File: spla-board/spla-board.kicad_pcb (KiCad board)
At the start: 4 copper layers, 165 x 107 mm, 285 parts, among them J1 USB_B_Micro, J12 J_POWER, J13 J_ANALOG, J14 J_AREF, J15 J_DPULL, J2 J_JTAG, J3 J_BODGE, J5 J_PPURESET, J6 J_SAMPLE, J7 Barrel_Jack, J8 J_AREF_AMP, J9 J_EXTRA, SW1 PTS645, SW2 SW_DPDT_x2, U1 LFE5U-45F-BG256, U10 SNES_PPU1, U11 SNES_PPU2, U12 VRAM, U13 VRAM, U14 TLV73311PDBV, U15 74LVC8T245, U16 74LVC8T245, U17 74LVC8T245, U2 FT2232H, U20 74LVC8T245, U22 74LVC8T245, U23 74LVC8T245, U24 74LVC8T245, U25 74LVC8T245, U26 74LVC8T245, U27 74LVC8T245, U28 74LVC8T245, U29 74LVC8T245, U3 93LC66B, U30 74LVC8T245, U31 74LVC8T245, U32 74LVC8T245, U4 74LVC1G17, U5 74LVC1G17, U51 ADC1173, U52 ADC1173, U53 ADC1173, U61 LMH6611, U62 LMH6611, U63 LMH6611, U7 ST1S10PHR, U74 LMH6611, U75 LMH6611, U76 TLV73333PDBV, U8 ST1S10PHR, U9 TLV73325PDBV, X1 FT5HNBPK12.0-T1

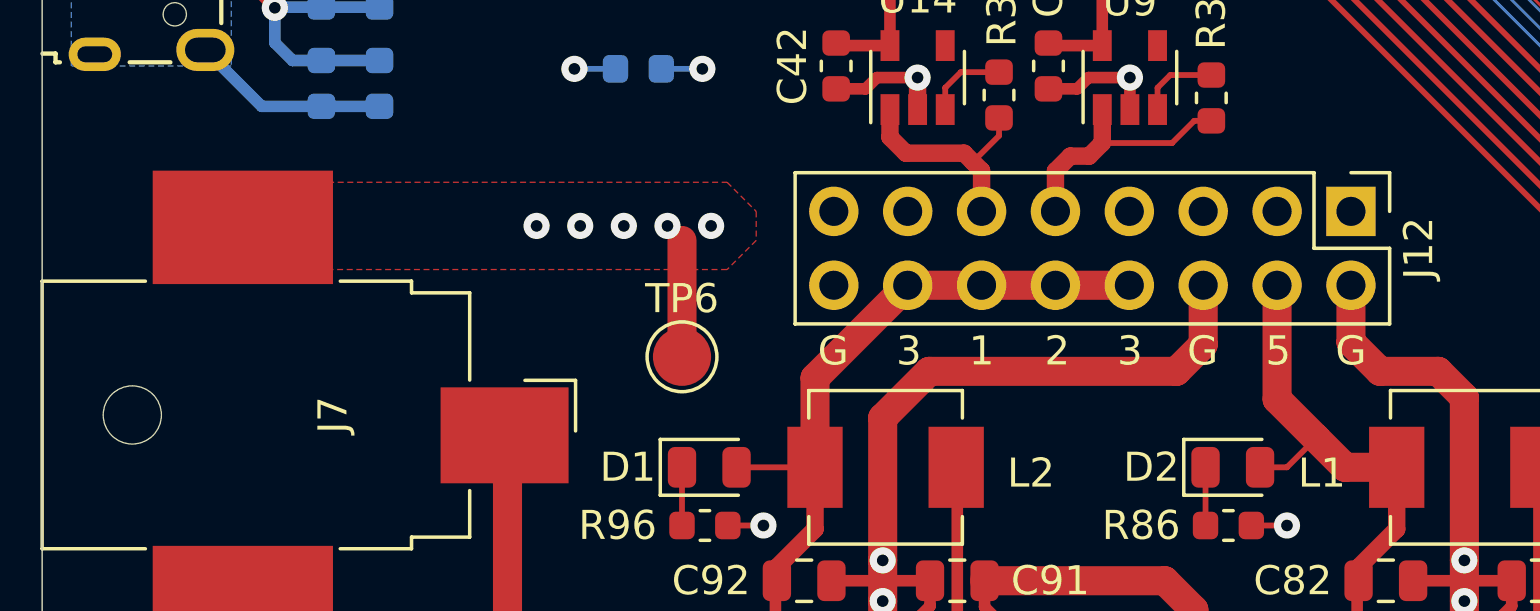
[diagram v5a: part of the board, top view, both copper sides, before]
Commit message: pcb: Remove GND via stitching, connect via J12 instead.
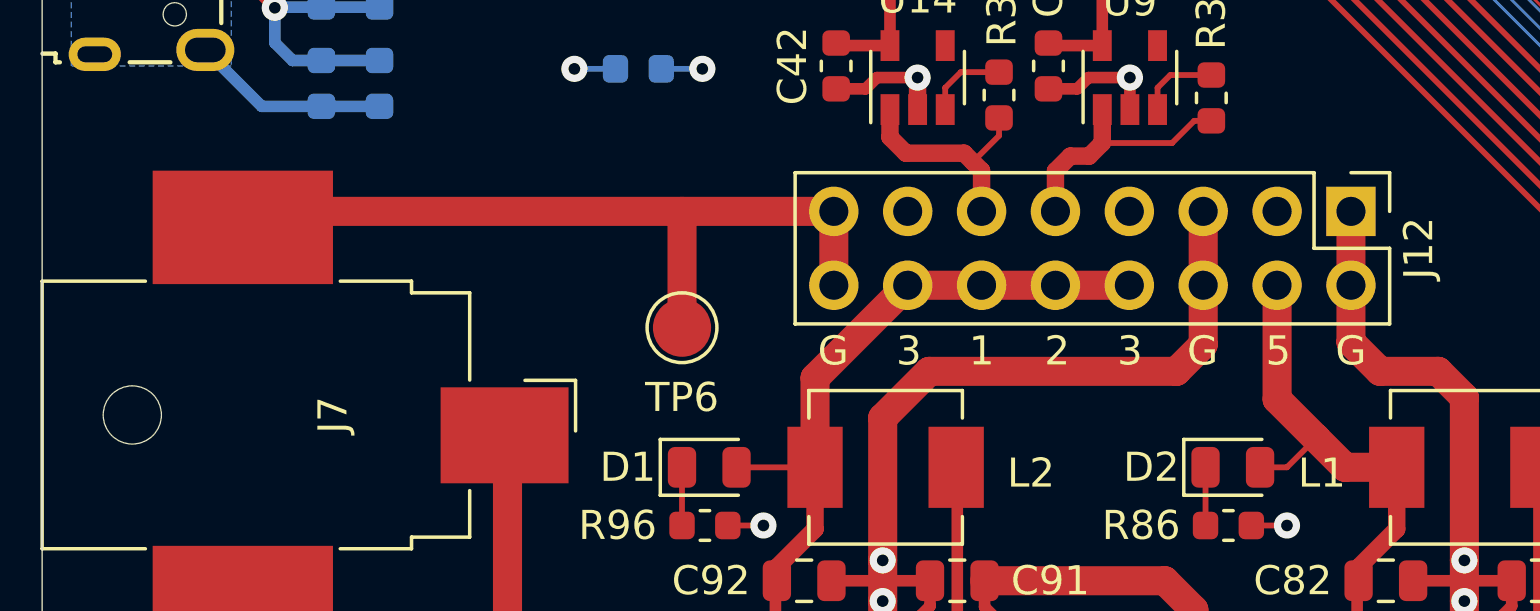
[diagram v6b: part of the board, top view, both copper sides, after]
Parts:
- moved TP6 1.00 mm to (75.0, 130.0)
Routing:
- net GND: track 526.5 -> 554.7 mm, vias 162 -> 157
- removed copper zone on F.Cu, net GND
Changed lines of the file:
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@@
     (thickness 1.6)
     (drawings 70)
-    (tracks 4560)
+    (tracks 4559)
     (zones 0)
     (modules 285)
@@
   )
   (module TestPoint:TestPoint_Pad_D2.0mm (layer F.Cu)
-    (at 75 131)
+    (at 75 130)
     (descr "SMD pad as test Point, diameter 2.0mm")
     (tags "test point SMD pad")
     (attr virtual)
-    (fp_text reference TP6 (at 0 -1.998) (layer F.SilkS)
+    (fp_text reference TP6 (at 0 2.4) (layer F.SilkS)
       (effects (font (size 1 1) (thickness 0.15)))
     )
@@
   (segment (start 90.2 106.8) (end 90.6 106.4) (width 0.4) (layer B.Cu) (net 1))
   (segment (start 90.2 107.4) (end 90.2 106.8) (width 0.4) (layer B.Cu) (net 1))
-  (segment (start 76 126.5) (end 76 126.5) (width 1) (layer F.Cu) (net 1))
   (segment (start 163.6875 85.2) (end 163.8 85.0875) (width 0.2) (layer B.Cu) (net 1))
   (segment (start 135 99.4) (end 133 99.4) (width 0.1) (layer F.Cu) (net 1))
@@
   (segment (start 61 120.2) (end 61 119) (width 0.4) (layer B.Cu) (net 1))
   (segment (start 61.6125 120.8125) (end 61 120.2) (width 0.4) (layer B.Cu) (net 1))
-  (via (at 76 126.5) (size 0.9) (drill 0.4) (layers F.Cu B.Cu) (net 1))
-  (via (at 74.5 126.5) (size 0.9) (drill 0.4) (layers F.Cu B.Cu) (net 1))
-  (via (at 73 126.5) (size 0.9) (drill 0.4) (layers F.Cu B.Cu) (net 1))
-  (via (at 71.5 126.5) (size 0.9) (drill 0.4) (layers F.Cu B.Cu) (net 1))
-  (via (at 70 126.5) (size 0.9) (drill 0.4) (layers F.Cu B.Cu) (net 1))
   (segment (start 77.7 115.0875) (end 77.8125 115.2) (width 0.2) (layer F.Cu) (net 1))
   (segment (start 77.7 113.7) (end 77.7 115.0875) (width 0.2) (layer F.Cu) (net 1))
@@
   (segment (start 135.8875 134.4125) (end 135.8875 134.4125) (width 0.2) (layer B.Cu) (net 1))
   (via (at 135.8875 134.4125) (size 0.9) (drill 0.4) (layers F.Cu B.Cu) (net 1))
-  (segment (start 75 127) (end 75 131) (width 1) (layer F.Cu) (net 1))
   (segment (start 61.9 99.475) (end 61.9 101) (width 0.2) (layer B.Cu) (net 1))
   (segment (start 64.5 103.6) (end 67.4 103.6) (width 0.2) (layer B.Cu) (net 1))
   (segment (start 61.9 101) (end 64.5 103.6) (width 0.2) (layer B.Cu) (net 1))
+  (segment (start 60.45 126) (end 59.9 126.55) (width 1) (layer F.Cu) (net 1))
+  (segment (start 80.22 126) (end 60.45 126) (width 1) (layer F.Cu) (net 1))
+  (segment (start 75 126) (end 75 130) (width 1) (layer F.Cu) (net 1))
+  (segment (start 80.22 126) (end 80.22 128.54) (width 1) (layer F.Cu) (net 1))
+  (segment (start 92.92 126) (end 92.92 128.54) (width 1) (layer F.Cu) (net 1))
+  (segment (start 98 126) (end 98 128.54) (width 1) (layer F.Cu) (net 1))
   (via (at 134.3 134.4) (size 0.9) (drill 0.4) (layers F.Cu B.Cu) (net 2))
   (via (at 96.2 102.4) (size 0.45) (drill 0.2) (layers F.Cu B.Cu) (net 2))
@@
       )
     )
-  )
-  (zone (net 1) (net_name GND) (layer F.Cu) (hatch edge 0.508)
-    (connect_pads (clearance 0.508))
-    (min_thickness 0.254)
-    (fill yes (arc_segments 32) (thermal_gap 0.508) (thermal_bridge_width 0.508))
-    (polygon
-      (pts
-        (xy 77.550858 127) (xy 76.550858 128) (xy 57.550858 128) (xy 57.550858 125) (xy 76.550858 125)
-        (xy 77.550858 126)
-      )
-    )

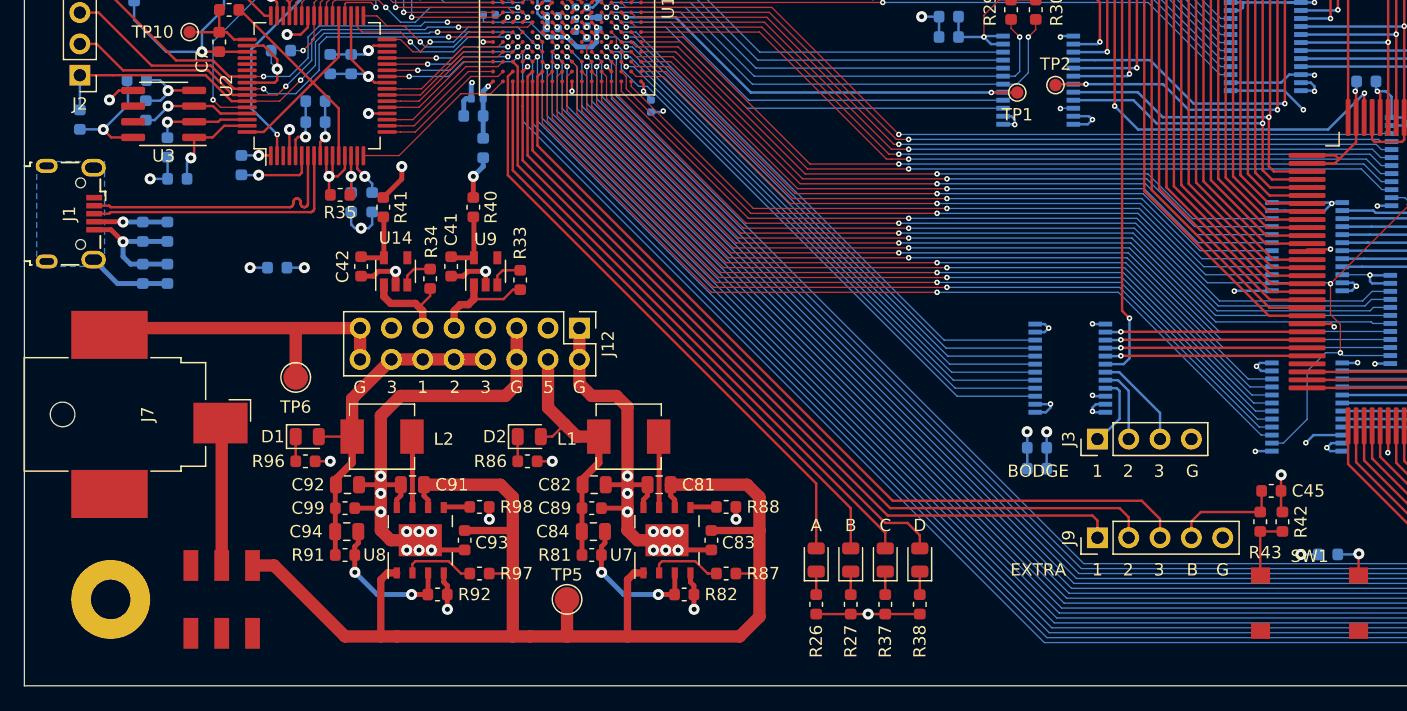
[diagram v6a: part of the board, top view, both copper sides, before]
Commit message: schematic/pcb: Remove bogus JTAG TMS pullup.
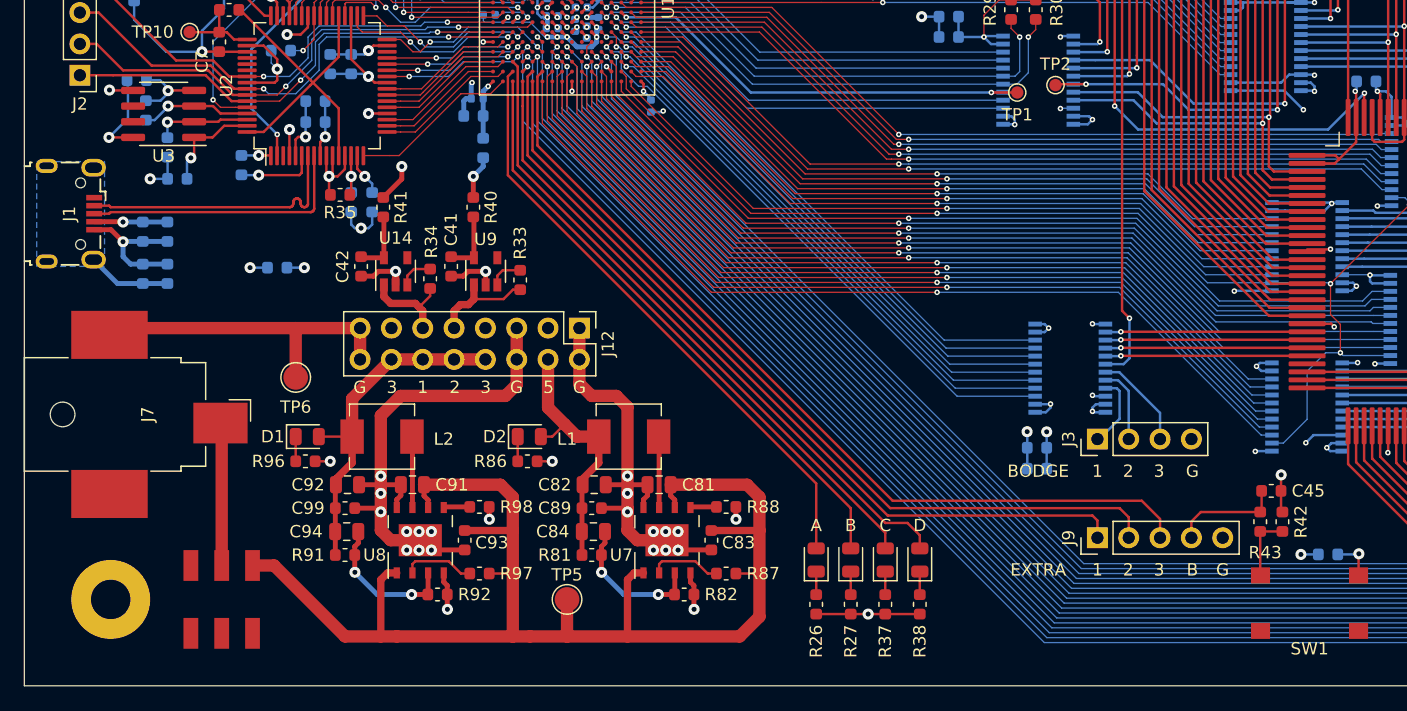
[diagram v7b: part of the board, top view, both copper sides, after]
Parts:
- removed R13: 10k, Resistor_SMD:R_0603_1608Metric
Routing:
- net JTAG_TMS: track 40.6 -> 37.8 mm
- net +3V3: track 158.0 -> 155.8 mm
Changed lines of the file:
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@@
     (thickness 1.6)
     (drawings 70)
-    (tracks 4559)
+    (tracks 4555)
     (zones 0)
-    (modules 285)
+    (modules 284)
     (nets 455)
   )
@@
   )
   (setup
-    (last_trace_width 1)
+    (last_trace_width 0.2)
     (user_trace_width 0.1)
     (user_trace_width 0.2)
@@
   (module SPLA:PTS645-SMTR92 (layer F.Cu)
     (at 157.2 148.3)
-    (fp_text reference SW1 (at 0 -3.8) (layer F.SilkS)
+    (fp_text reference SW1 (at 0 3.7) (layer F.SilkS)
       (effects (font (size 1 1) (thickness 0.15)))
     )
@@
     )
   )
-  (module Resistor_SMD:R_0603_1608Metric (layer B.Cu)
-    (at 57.5 109.1 90)
-    (descr "Resistor SMD 0603 (1608 Metric), square (rectangular) end terminal, IPC_7351 nominal, (Body size source: http://www.tortai-tech.com/upload/download/2011102023233369053.pdf), generated with kicad-footprint-generator")
-    (tags resistor)
-    (attr smd)
-    (fp_text reference R13 (at 0 -1.524 90) (layer B.SilkS)
-      (effects (font (size 1 1) (thickness 0.15)) (justify mirror))
-    )
-    (fp_text value 10k (at 0 -1.43 90) (layer B.Fab)
-      (effects (font (size 1 1) (thickness 0.15)) (justify mirror))
-    )
-    (fp_line (start -0.8 -0.4) (end -0.8 0.4) (layer B.Fab) (width 0.1))
-    (fp_line (start -0.8 0.4) (end 0.8 0.4) (layer B.Fab) (width 0.1))
-    (fp_line (start 0.8 0.4) (end 0.8 -0.4) (layer B.Fab) (width 0.1))
-    (fp_line (start 0.8 -0.4) (end -0.8 -0.4) (layer B.Fab) (width 0.1))
-    (fp_line (start -0.162779 0.51) (end 0.162779 0.51) (layer B.SilkS) (width 0.12))
-    (fp_line (start -0.162779 -0.51) (end 0.162779 -0.51) (layer B.SilkS) (width 0.12))
-    (fp_line (start -1.48 -0.73) (end -1.48 0.73) (layer B.CrtYd) (width 0.05))
-    (fp_line (start -1.48 0.73) (end 1.48 0.73) (layer B.CrtYd) (width 0.05))
-    (fp_line (start 1.48 0.73) (end 1.48 -0.73) (layer B.CrtYd) (width 0.05))
-    (fp_line (start 1.48 -0.73) (end -1.48 -0.73) (layer B.CrtYd) (width 0.05))
-    (fp_text user %R (at 0 0 90) (layer B.Fab)
-      (effects (font (size 0.4 0.4) (thickness 0.06)) (justify mirror))
-    )
-    (pad 2 smd roundrect (at 0.7875 0 90) (size 0.875 0.95) (layers B.Cu B.Paste B.Mask) (roundrect_rratio 0.25)
-      (net 6 JTAG_TMS))
-    (pad 1 smd roundrect (at -0.7875 0 90) (size 0.875 0.95) (layers B.Cu B.Paste B.Mask) (roundrect_rratio 0.25)
-      (net 2 +3V3))
-    (model ${KISYS3DMOD}/Resistor_SMD.3dshapes/R_0603_1608Metric.wrl
-      (at (xyz 0 0 0))
-      (scale (xyz 1 1 1))
-      (rotate (xyz 0 0 0))
-    )
-  )
   (module Resistor_SMD:R_0603_1608Metric (layer F.Cu)
     (at 109.9 145.9 180)
@@
   (segment (start 79.4875 104.1875) (end 79.4875 100.675) (width 0.2) (layer F.Cu) (net 1))
   (segment (start 80.9 105.6) (end 79.4875 104.1875) (width 0.2) (layer F.Cu) (net 1))
-  (via (at 59.9 107.5) (size 0.9) (drill 0.4) (layers F.Cu B.Cu) (net 1))
-  (segment (start 61.8165 106.731) (end 60.669 106.731) (width 0.2) (layer F.Cu) (net 1))
-  (segment (start 60.669 106.731) (end 59.9 107.5) (width 0.2) (layer F.Cu) (net 1))
   (segment (start 98.615 100.815) (end 98.6 100.8) (width 0.4) (layer B.Cu) (net 1))
   (segment (start 99.55 100.815) (end 98.615 100.815) (width 0.4) (layer B.Cu) (net 1))
@@
   (segment (start 92.92 126) (end 92.92 128.54) (width 1) (layer F.Cu) (net 1))
   (segment (start 98 126) (end 98 128.54) (width 1) (layer F.Cu) (net 1))
+  (segment (start 59.931 106.731) (end 61.8165 106.731) (width 0.2) (layer F.Cu) (net 1))
+  (via (at 59.9 106.7) (size 0.9) (drill 0.4) (layers F.Cu B.Cu) (net 1))
+  (segment (start 59.9 106.7) (end 59.931 106.731) (width 0.2) (layer F.Cu) (net 1))
   (via (at 134.3 134.4) (size 0.9) (drill 0.4) (layers F.Cu B.Cu) (net 2))
   (via (at 96.2 102.4) (size 0.45) (drill 0.2) (layers F.Cu B.Cu) (net 2))
@@
   (segment (start 75.7 121.1) (end 74.2875 121.1) (width 0.2) (layer B.Cu) (net 2))
   (via (at 75.7 121.1) (size 0.9) (drill 0.4) (layers F.Cu B.Cu) (net 2))
-  (segment (start 59.3875 109.8875) (end 57.5 109.8875) (width 0.2) (layer B.Cu) (net 2))
-  (segment (start 61.325 105.925) (end 61.325 105.9) (width 0.2) (layer B.Cu) (net 2))
-  (segment (start 59.4 109.9) (end 60.041 110.541) (width 0.2) (layer F.Cu) (net 2))
-  (via (at 59.4 109.9) (size 0.9) (drill 0.4) (layers F.Cu B.Cu) (net 2))
-  (segment (start 59.4 109.9) (end 59.3875 109.8875) (width 0.2) (layer B.Cu) (net 2))
-  (segment (start 60.041 110.541) (end 61.8165 110.541) (width 0.2) (layer F.Cu) (net 2))
-  (segment (start 59.4 109.9) (end 61.4 107.9) (width 0.2) (layer B.Cu) (net 2))
-  (segment (start 61.4 107.9) (end 61.4 106) (width 0.2) (layer B.Cu) (net 2))
-  (segment (start 61.4 106) (end 61.325 105.925) (width 0.2) (layer B.Cu) (net 2))
+  (segment (start 59.859 110.541) (end 61.8165 110.541) (width 0.2) (layer F.Cu) (net 2))
+  (via (at 59.859 110.541) (size 0.9) (drill 0.4) (layers F.Cu B.Cu) (net 2))
+  (segment (start 61.4 109) (end 59.859 110.541) (width 0.2) (layer B.Cu) (net 2))
+  (segment (start 61.4 106) (end 61.4 109) (width 0.2) (layer B.Cu) (net 2))
+  (segment (start 61.325 105.9) (end 61.325 105.925) (width 0.2) (layer B.Cu) (net 2))
+  (segment (start 61.325 105.925) (end 61.4 106) (width 0.2) (layer B.Cu) (net 2))
   (segment (start 72.4 110.1) (end 71.0625 110.1) (width 0.2) (layer F.Cu) (net 3))
   (segment (start 76.2 106.3) (end 72.4 110.1) (width 0.2) (layer F.Cu) (net 3))
@@
   (segment (start 85.9 102) (end 85.8 102.1) (width 0.1) (layer B.Cu) (net 6))
   (segment (start 77.3 102.1) (end 76.6 102.8) (width 0.1) (layer B.Cu) (net 6))
-  (segment (start 57.5 108.3125) (end 57.5 105.5) (width 0.2) (layer B.Cu) (net 6))
   (segment (start 60.2 105.5) (end 57.5 105.5) (width 0.2) (layer F.Cu) (net 6))
   (segment (start 72.4 105.6) (end 70.3375 105.6) (width 0.1) (layer F.Cu) (net 7))

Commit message: schematic: Swap FTDI REF resistor from 5% (oops) to 1%.
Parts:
- R6: value 12k -> 12k, 1%
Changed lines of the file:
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@@
       (effects (font (size 1 1) (thickness 0.15)) (justify mirror))
     )
-    (fp_text value 12k (at 0 -1.43 90) (layer B.Fab)
+    (fp_text value "12k, 1%" (at 0 -1.43 90) (layer B.Fab)
       (effects (font (size 1 1) (thickness 0.15)) (justify mirror))
     )
